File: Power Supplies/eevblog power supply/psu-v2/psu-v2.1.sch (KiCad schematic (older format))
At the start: 41 parts, among them Q1 3904, Q2 3904, SW1 SW_SPST, U1 TL431LP, U2 ICL7660, U3 TL431LP, U4 LM324, U5 LM1117

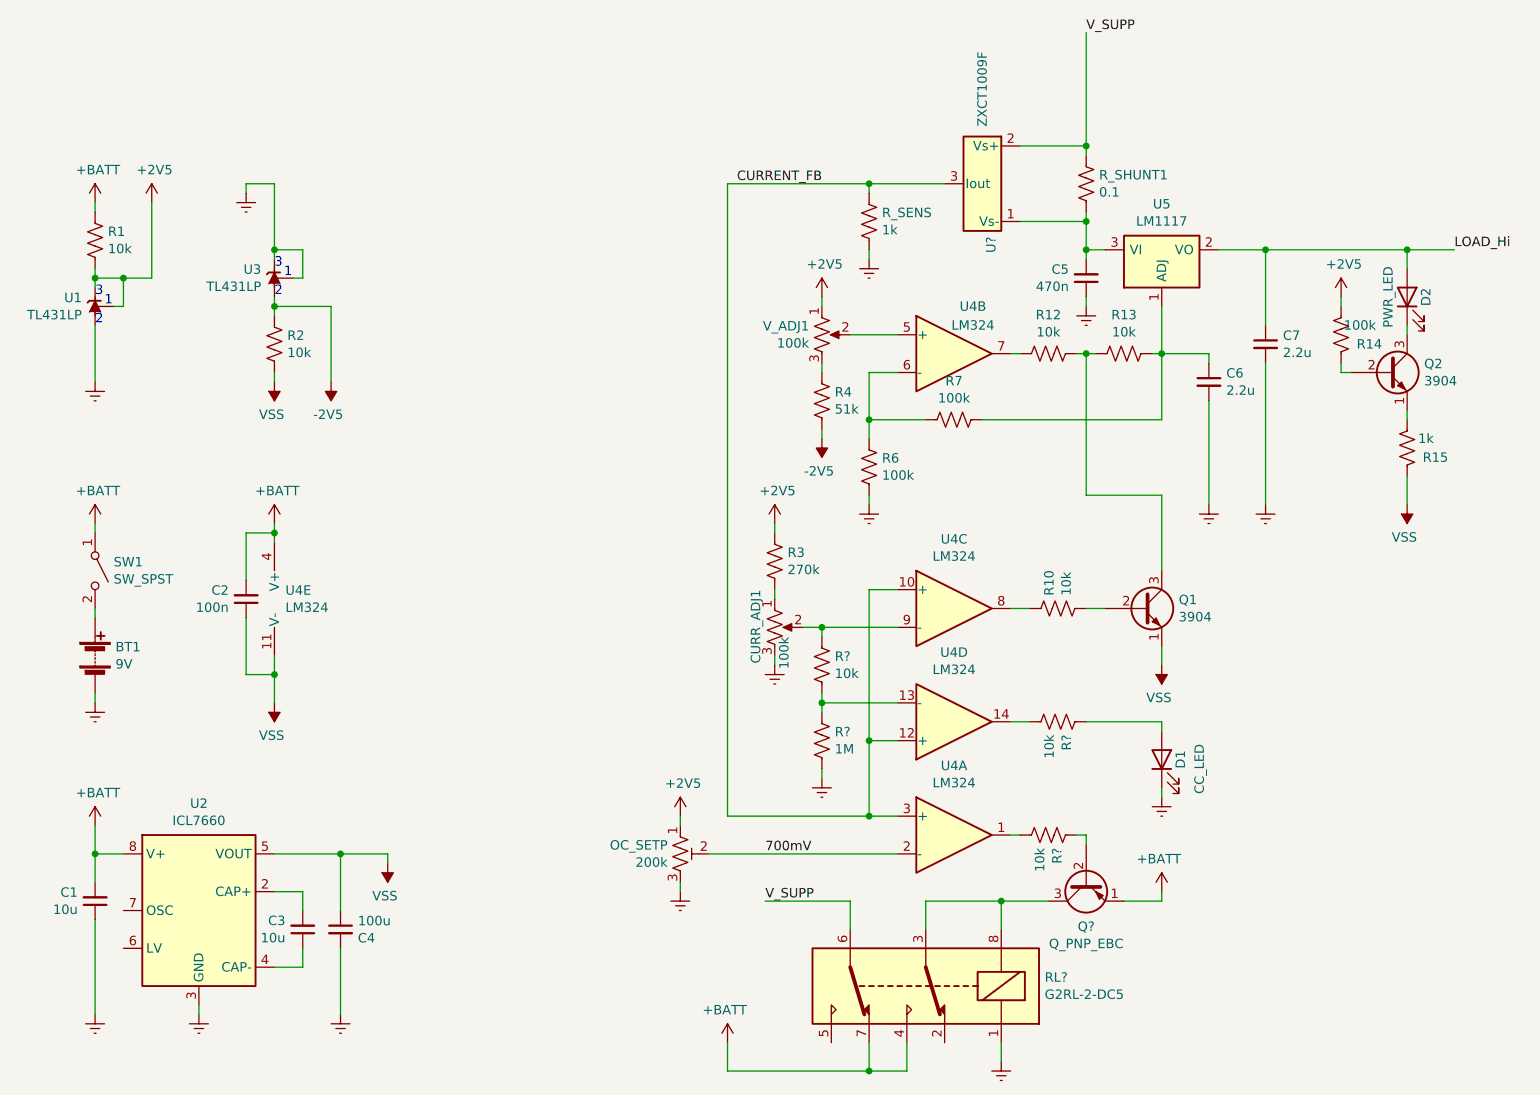
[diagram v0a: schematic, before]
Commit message: updates to voltage fedback
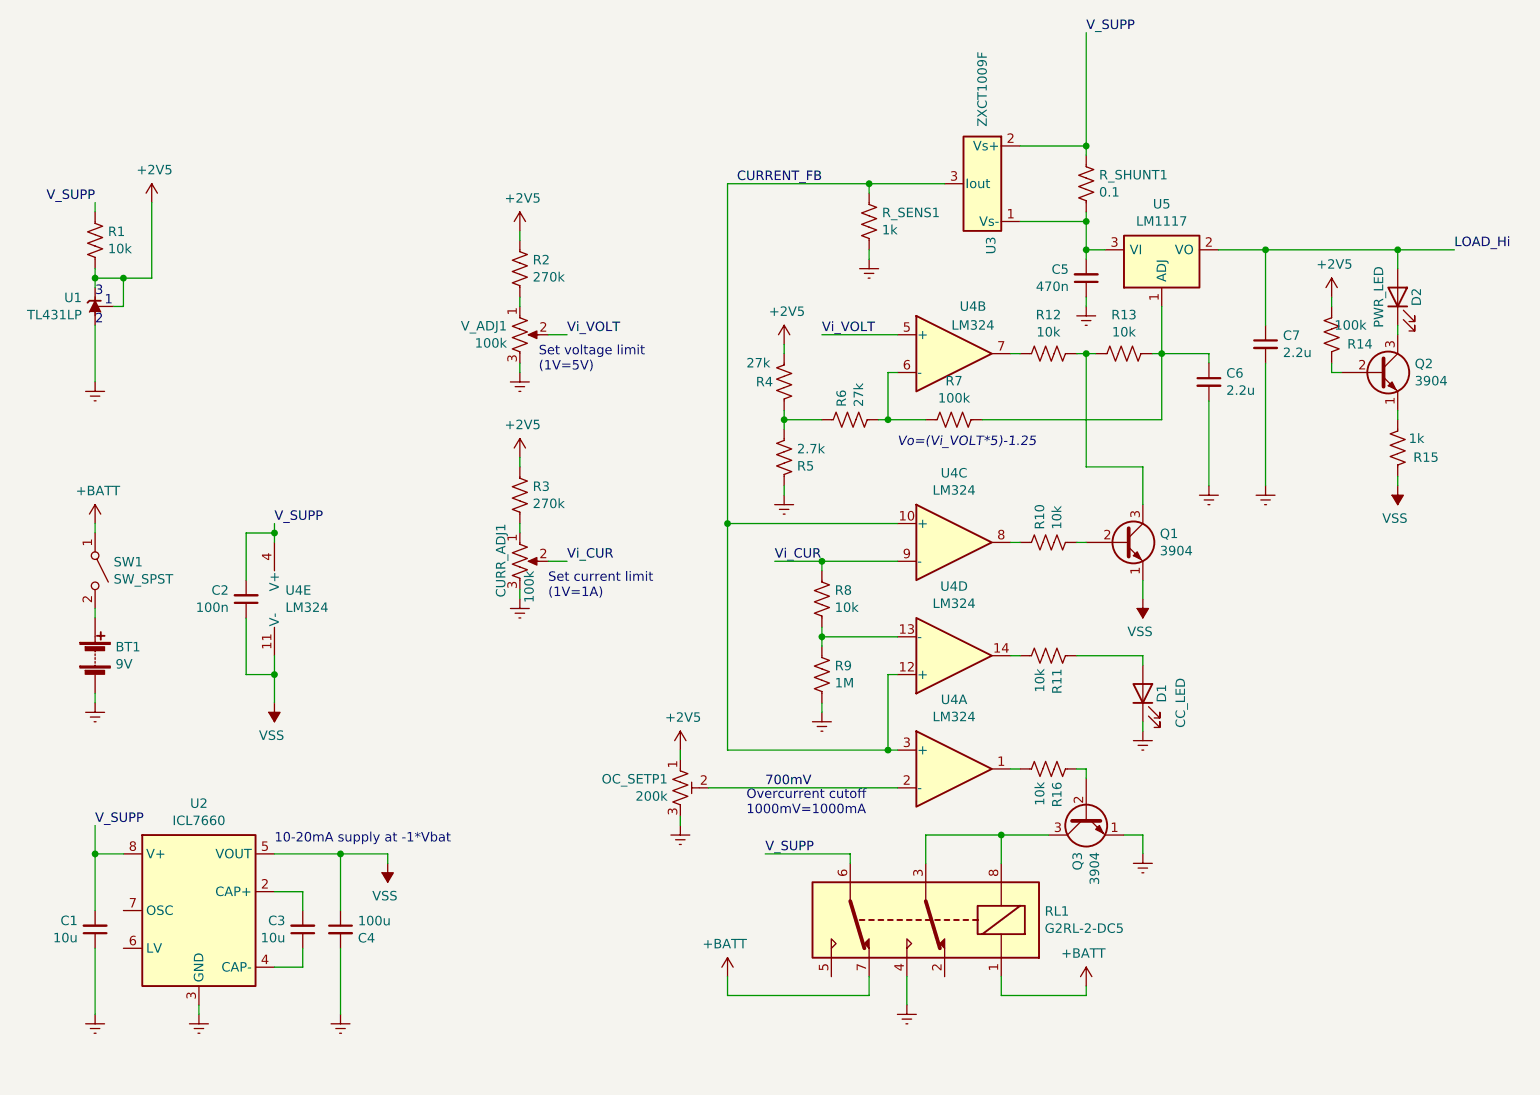
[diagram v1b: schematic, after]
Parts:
- removed Q?: Q_PNP_EBC, symbol Device:Q_PNP_EBC
- removed U3: TL431LP, Package_TO_SOT_THT:TO-92_Inline, symbol Reference_Voltage:TL431LP
- added Q3: 3904, Package_TO_SOT_THT:TO-92L_Inline, symbol Device:Q_NPN_EBC
- added R5: 2.7k, Resistor_THT:R_Axial_DIN0204_L3.6mm_D1.6mm_P5.08mm_Horizontal, symbol Device:R_US
- R2: value 10k -> 270k
- R4: value 51k -> 27k
- R6: value 100k -> 27k
- gave numbers to parts that had none: 6
- renumbered OC_SETP to OC_SETP1, R_SENS to R_SENS1
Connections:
- net -2V5 is gone; now on net +2V5: R2.2, R4.1
- net +2V5: no longer V_ADJ1.1
- net +BATT: now also RL1.1; no longer C1.2, C2.2, R1.2, RL1.4, U2.8 (V+), U4.4 (V+)
- net Earth: now also RL1.4, V_ADJ1.3, Q3.1 (E), R5.2; no longer R6.1, RL1.1
- net VSS: no longer R2.1
- net V_SUPP: now also C1.2, C2.2, R1.2, U2.8 (V+), U4.4 (V+)
- net Vi_VOLT: now reaches U4.5 (+), V_ADJ1.2
- net at R7.1, U4.6 (-): now also R6.1; no longer R6.2
- net Vi_CUR: now reaches CURR_ADJ1.2, R8.2, U4.9 (-)
- net at R4.2: now also R6.2, R5.1; no longer V_ADJ1.3
- net at RL1.3, RL1.8: now also Q3.3 (C)
- net at R16.1: now also Q3.2 (B)
- new net: R2.1, V_ADJ1.1
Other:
- note added: "10-20mA supply at -1*Vbat"
- note added: "Overcurrent cutoff\n1000mV=1000mA"
- note added: "Set current limit\n(1V=1A)"
- note added: "Set voltage limit\n(1V=5V)"
- note added: "Vo=(Vi_VOLT*5)-1.25"
- moved on the sheet: C1, CURR_ADJ1, D1, D2, OC_SETP1, Q1, Q2, R10, R11, R14, R15, R16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

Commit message: update voltage feedback
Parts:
- removed R5: 2.7k, Resistor_THT:R_Axial_DIN0204_L3.6mm_D1.6mm_P5.08mm_Horizontal, symbol Device:R_US
- removed R7: 100k, Resistor_THT:R_Axial_DIN0204_L3.6mm_D1.6mm_P5.08mm_Horizontal, symbol Device:R_US
- added R_GAIN: 500k, symbol Device:R_POT_TRIM_US
- added R_OFFSET: 10k, symbol Device:R_POT_TRIM_US
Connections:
- net Earth: now also R_OFFSET.2, R_OFFSET.3
- net at R6.1, U4.6 (-): now also R_GAIN.1
- net at C6.1, R13.2, U5.1 (ADJ): now also R_GAIN.2, R_GAIN.3
- net at R4.2, R6.2: now also R_OFFSET.1
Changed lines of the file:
@@
 	0    1    1    0
-$EndComp
-$Comp
-L Device:R_US R7
-U 1 1 60BE0EC9
-P 6050 3050
-F 0 "R7" V 6255 3050 50  0000 C CNN
-F 1 "100k" V 6164 3050 50  0000 C CNN
-F 2 "Resistor_THT:R_Axial_DIN0204_L3.6mm_D1.6mm_P5.08mm_Horizontal" V 6090 3040 50  0001 C CNN
-F 3 "~" H 6050 3050 50  0001 C CNN
-	1    6050 3050
-	0    -1   -1   0
 $EndComp
 Wire Wire Line
@@
 $EndComp
 $Comp
-L Device:R_US R5
-U 1 1 61FB8A2D
-P 5150 3250
-F 0 "R5" H 5082 3204 50  0000 R CNN
-F 1 "2.7k" H 5082 3295 50  0000 R CNN
-F 2 "Resistor_THT:R_Axial_DIN0204_L3.6mm_D1.6mm_P5.08mm_Horizontal" V 5190 3240 50  0001 C CNN
-F 3 "~" H 5150 3250 50  0001 C CNN
-	1    5150 3250
-	-1   0    0    -1
-$EndComp
-$Comp
 L power:Earth #PWR021
 U 1 1 61FC367A
@@
 	1    0    0    -1
 $EndComp
-Wire Wire Line
-	5150 3450 5150 3400
 Wire Wire Line
 	5150 2700 5150 2650
@@
 Wire Wire Line
 	3750 2050 3750 2100
-Text Notes 5750 3200 0    50   Italic 0
+Text Notes 5350 2450 0    50   Italic 0
 Vo=(Vi_VOLT*5)-1.25
 Text Notes 4950 5150 0    50   ~ 0
@@
 Wire Wire Line
 	8400 2150 8700 2150
+$Comp
+L Device:R_POT_TRIM_US R_OFFSET
+U 1 1 61F9D71C
+P 5150 3250
+F 0 "R_OFFSET" H 5083 3296 50  0000 R CNN
+F 1 "10k" H 5083 3205 50  0000 R CNN
+F 2 "" H 5150 3250 50  0001 C CNN
+F 3 "~" H 5150 3250 50  0001 C CNN
+	1    5150 3250
+	1    0    0    -1
+$EndComp
+Wire Wire Line
+	5150 3450 5150 3400
+Wire Wire Line
+	5150 3400 5300 3400
+Wire Wire Line
+	5300 3400 5300 3250
+Connection ~ 5150 3400
+$Comp
+L Device:R_POT_TRIM_US R_GAIN
+U 1 1 61FBFBF0
+P 6050 3050
+F 0 "R_GAIN" V 5950 3350 50  0000 R CNN
+F 1 "500k" V 5950 3050 50  0000 R CNN
+F 2 "" H 6050 3050 50  0001 C CNN
+F 3 "~" H 6050 3050 50  0001 C CNN
+	1    6050 3050
+	0    -1   -1   0
+$EndComp
+Wire Wire Line
+	6050 2900 6200 2900
+Wire Wire Line
+	6200 2900 6200 3050
+Connection ~ 6200 3050
 $EndSCHEMATC

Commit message: add new circuits
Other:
- note added: "140mV"
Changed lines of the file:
@@
 	6200 2900 6200 3050
 Connection ~ 6200 3050
+Text Notes 5150 3050 0    50   ~ 0
+140mV
 $EndSCHEMATC
